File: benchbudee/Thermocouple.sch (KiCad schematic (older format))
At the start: 0 parts

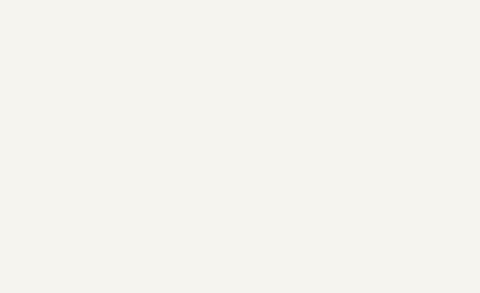
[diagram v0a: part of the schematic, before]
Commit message: Added signals
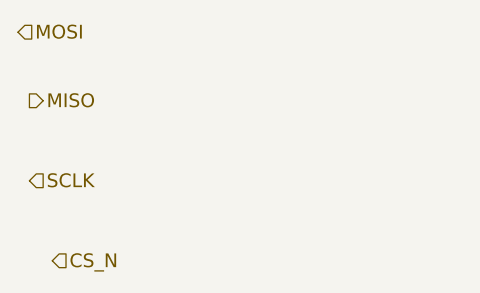
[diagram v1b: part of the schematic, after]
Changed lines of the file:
@@
 Text HLabel 8800 2850 2    60   Input ~ 0
 TC IN -
+Text HLabel 1650 2050 2    60   Input ~ 0
+MOSI
+Text HLabel 1700 2350 2    60   Output ~ 0
+MISO
+Text HLabel 1700 2700 2    60   Input ~ 0
+SCLK
+Text HLabel 1800 3050 2    60   Input ~ 0
+CS_N
 $EndSCHEMATC

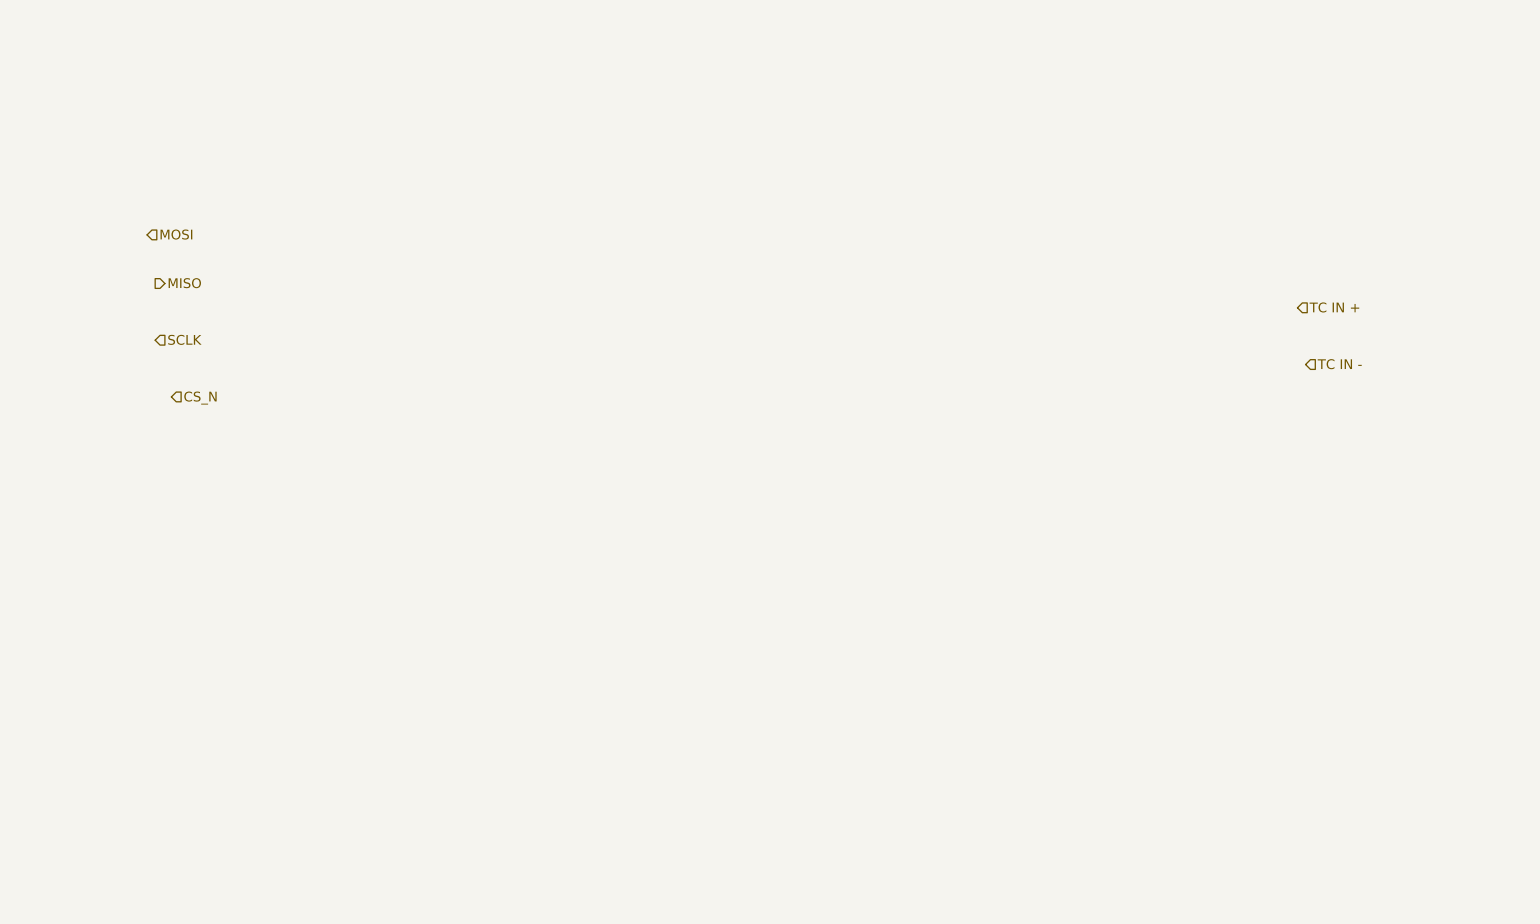
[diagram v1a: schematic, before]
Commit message: Added block diagram and thermocouple schematic
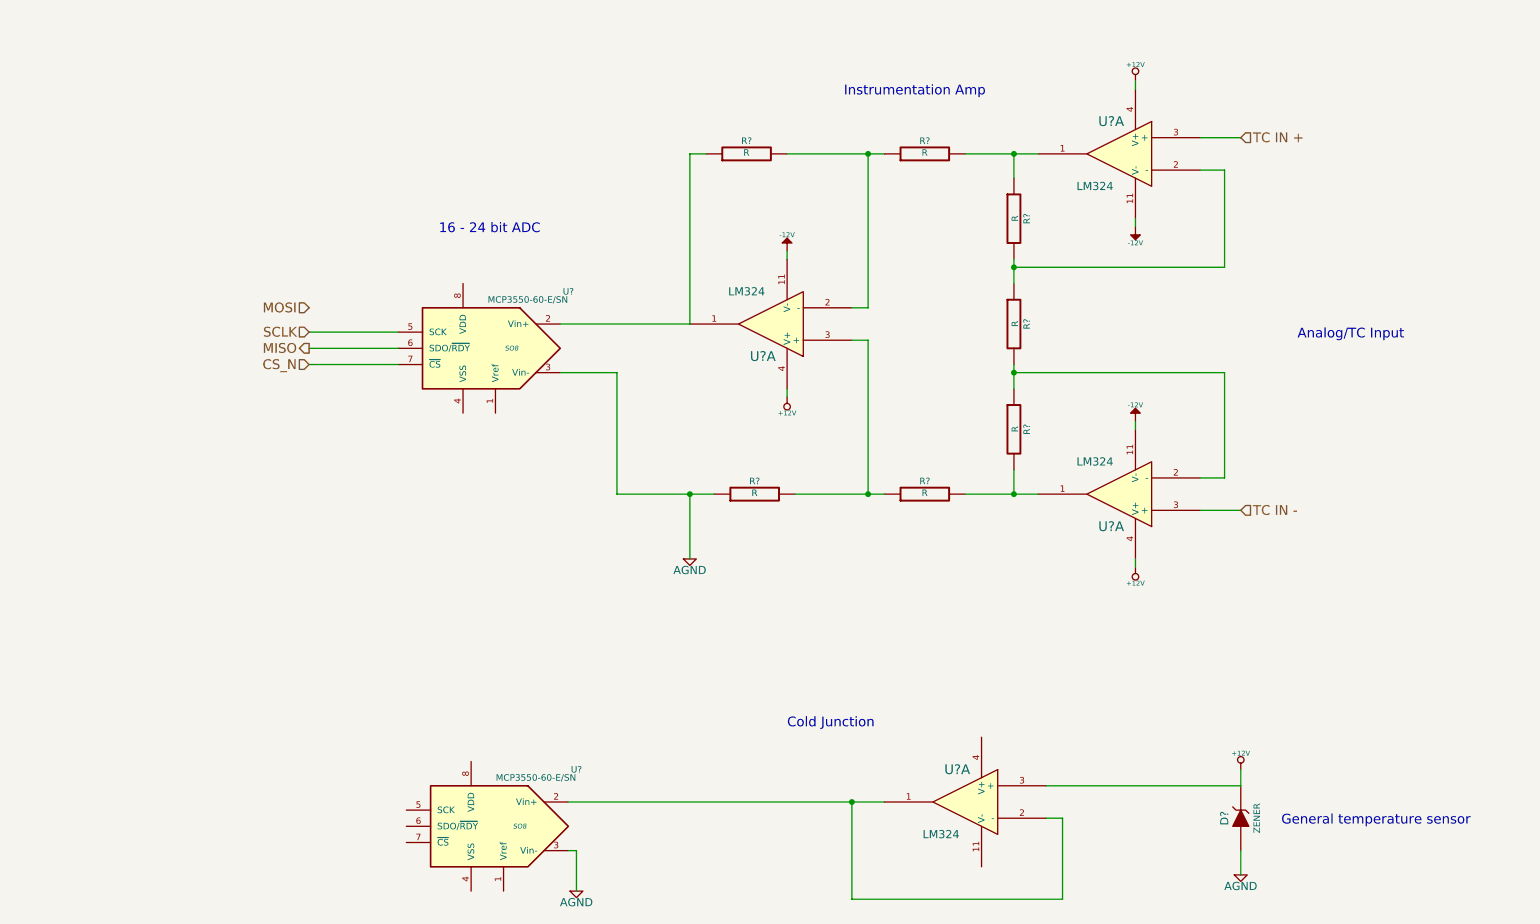
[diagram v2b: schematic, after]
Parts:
- added D?: ZENER, ~, symbol ZENER
- added R? (x7): R, ~, symbol R
- added U? (x4): LM324, symbol LM324
- added U? (x2): MCP3550-60-E/SN, SO8, symbol MCP3550-60-E/SN
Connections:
- net CS_N: now also U?.7 (~CS~)
- net MISO: now also U?.6 (SDO/~RDY~)
- net SCLK: now also U?.5 (SCK)
- net TC IN +: now also U?.3 (+)
- net TC IN -: now also U?.3 (+)
- new net: R?.1, R?.2, U?.1
- new net: R?.1, R?.2, U?.2 (-) (x3)
- new net: R?.2, R?.2, U?.1
- new net: R?.1, U?.1, U?.2 (Vin+)
- new net: R?.1, R?.2, U?.3 (+)
- new net: U?.1, U?.2 (-), U?.2 (Vin+)
- new net +12V: D?.2 (K), U?.3 (+), U?.4 (V+), U?.4 (V+), U?.4 (V+)
- new net -12V: U?.11 (V-), U?.11 (V-), U?.11 (V-)
- new net AGND: D?.1 (A), R?.1, U?.3 (Vin-), U?.3 (Vin-)
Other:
- note added: "16 - 24 bit ADC"
- note added: "Analog/TC Input"
- note added: "Cold Junction"
- note added: "General temperature sensor"
- note added: "Instrumentation Amp"

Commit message: Relay module footprints done
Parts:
- gave numbers to parts that had none: 11
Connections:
- net +12V: now also U4.5 (+); no longer U4.3 (+)
- net TC IN +: now also U4.10 (+); no longer U4.3 (+)
- net TC IN -: now also U4.12 (+); no longer U4.3 (+)
- net at R11.1, R9.2: now also U4.8; no longer U4.1
- net at R11.2, R12.1: now also U4.9 (-); no longer U4.2 (-)
- net at R10.2, R13.2: now also U4.14; no longer U4.1
- net at R12.2, R13.1: now also U4.13 (-); no longer U4.2 (-)
- new net: U3.2 (Vin+), U4.6 (-), U4.7
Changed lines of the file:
@@
 CS_N
 $Comp
-L LM324 U?
-U 1 1 52FAF263
+L LM324 U4
+U 3 1 52FAF263
 P 7650 1550
-F 0 "U?" H 7700 1750 60  0000 C CNN
+F 0 "U4" H 7700 1750 60  0000 C CNN
 F 1 "LM324" H 7800 1350 50  0000 C CNN
 F 2 "" H 7650 1550 60  0000 C CNN
 F 3 "" H 7650 1550 60  0000 C CNN
-	1    7650 1550
+	3    7650 1550
 	-1   0    0    -1
 $EndComp
 $Comp
-L LM324 U?
-U 1 1 52FAF27A
+L LM324 U4
+U 4 1 52FAF27A
 P 7650 3650
-F 0 "U?" H 7700 3850 60  0000 C CNN
+F 0 "U4" H 7700 3850 60  0000 C CNN
 F 1 "LM324" H 7800 3450 50  0000 C CNN
 F 2 "" H 7650 3650 60  0000 C CNN
 F 3 "" H 7650 3650 60  0000 C CNN
-	1    7650 3650
-	-1   0    0    1
-$EndComp
-$Comp
-L LM324 U?
+	4    7650 3650
+	-1   0    0    1
+$EndComp
+$Comp
+L LM324 U4
 U 1 1 52FAF280
 P 5500 2600
-F 0 "U?" H 5550 2800 60  0000 C CNN
+F 0 "U4" H 5550 2800 60  0000 C CNN
 F 1 "LM324" H 5650 2400 50  0000 C CNN
 F 2 "" H 5500 2600 60  0000 C CNN
@@
 $EndComp
 $Comp
-L LM324 U?
-U 1 1 52FAF286
+L LM324 U4
+U 2 1 52FAF286
 P 6700 5550
-F 0 "U?" H 6750 5750 60  0000 C CNN
+F 0 "U4" H 6750 5750 60  0000 C CNN
 F 1 "LM324" H 6850 5350 50  0000 C CNN
 F 2 "" H 6700 5550 60  0000 C CNN
 F 3 "" H 6700 5550 60  0000 C CNN
-	1    6700 5550
+	2    6700 5550
 	-1   0    0    -1
 $EndComp
 $Comp
-L R R?
+L R R12
 U 1 1 52FAF2B2
 P 7000 2600
-F 0 "R?" V 7080 2600 40  0000 C CNN
+F 0 "R12" V 7080 2600 40  0000 C CNN
 F 1 "R" V 7007 2601 40  0000 C CNN
 F 2 "~" V 6930 2600 30  0000 C CNN
@@
 $EndComp
 $Comp
-L R R?
+L R R11
 U 1 1 52FAF2BF
 P 7000 1950
-F 0 "R?" V 7080 1950 40  0000 C CNN
+F 0 "R11" V 7080 1950 40  0000 C CNN
 F 1 "R" V 7007 1951 40  0000 C CNN
 F 2 "~" V 6930 1950 30  0000 C CNN
@@
 $EndComp
 $Comp
-L R R?
+L R R13
 U 1 1 52FAF2CF
 P 7000 3250
-F 0 "R?" V 7080 3250 40  0000 C CNN
+F 0 "R13" V 7080 3250 40  0000 C CNN
 F 1 "R" V 7007 3251 40  0000 C CNN
 F 2 "~" V 6930 3250 30  0000 C CNN
@@
 $EndComp
 $Comp
-L R R?
+L R R9
 U 1 1 52FAF2EA
 P 6450 1550
-F 0 "R?" V 6530 1550 40  0000 C CNN
+F 0 "R9" V 6530 1550 40  0000 C CNN
 F 1 "R" V 6457 1551 40  0000 C CNN
 F 2 "~" V 6380 1550 30  0000 C CNN
@@
 $EndComp
 $Comp
-L R R?
+L R R7
 U 1 1 52FAF2F0
 P 5350 1550
-F 0 "R?" V 5430 1550 40  0000 C CNN
+F 0 "R7" V 5430 1550 40  0000 C CNN
 F 1 "R" V 5357 1551 40  0000 C CNN
 F 2 "~" V 5280 1550 30  0000 C CNN
@@
 $EndComp
 $Comp
-L R R?
+L R R8
 U 1 1 52FAF2F6
 P 5400 3650
-F 0 "R?" V 5480 3650 40  0000 C CNN
+F 0 "R8" V 5480 3650 40  0000 C CNN
 F 1 "R" V 5407 3651 40  0000 C CNN
 F 2 "~" V 5330 3650 30  0000 C CNN
@@
 $EndComp
 $Comp
-L R R?
+L R R10
 U 1 1 52FAF2FC
 P 6450 3650
-F 0 "R?" V 6530 3650 40  0000 C CNN
+F 0 "R10" V 6530 3650 40  0000 C CNN
 F 1 "R" V 6457 3651 40  0000 C CNN
 F 2 "~" V 6380 3650 30  0000 C CNN
@@
 $EndComp
 $Comp
-L -12V #PWR?
+L -12V #PWR01
 U 1 1 52FAF3D3
 P 5600 2150
-F 0 "#PWR?" H 5600 2280 20  0001 C CNN
+F 0 "#PWR01" H 5600 2280 20  0001 C CNN
 F 1 "-12V" H 5600 2250 30  0000 C CNN
 F 2 "" H 5600 2150 60  0000 C CNN
@@
 $EndComp
 $Comp
-L -12V #PWR?
+L -12V #PWR02
 U 1 1 52FAF3E0
 P 7750 2000
-F 0 "#PWR?" H 7750 2130 20  0001 C CNN
+F 0 "#PWR02" H 7750 2130 20  0001 C CNN
 F 1 "-12V" H 7750 2100 30  0000 C CNN
 F 2 "" H 7750 2000 60  0000 C CNN
@@
 $EndComp
 $Comp
-L -12V #PWR?
+L -12V #PWR03
 U 1 1 52FAF3E6
 P 7750 3200
-F 0 "#PWR?" H 7750 3330 20  0001 C CNN
+F 0 "#PWR03" H 7750 3330 20  0001 C CNN
 F 1 "-12V" H 7750 3300 30  0000 C CNN
 F 2 "" H 7750 3200 60  0000 C CNN
@@
 $EndComp
 $Comp
-L +12V #PWR?
+L +12V #PWR04
 U 1 1 52FBAE4E
 P 5600 3050
-F 0 "#PWR?" H 5600 3000 20  0001 C CNN
+F 0 "#PWR04" H 5600 3000 20  0001 C CNN
 F 1 "+12V" H 5600 3150 30  0000 C CNN
 F 2 "" H 5600 3050 60  0000 C CNN
@@
 $EndComp
 $Comp
-L +12V #PWR?
+L +12V #PWR05
 U 1 1 52FBAE5B
 P 7750 4100
-F 0 "#PWR?" H 7750 4050 20  0001 C CNN
+F 0 "#PWR05" H 7750 4050 20  0001 C CNN
 F 1 "+12V" H 7750 4200 30  0000 C CNN
 F 2 "" H 7750 4100 60  0000 C CNN
@@
 $EndComp
 $Comp
-L +12V #PWR?
+L +12V #PWR06
 U 1 1 52FBAE63
 P 7750 1100
-F 0 "#PWR?" H 7750 1050 20  0001 C CNN
+F 0 "#PWR06" H 7750 1050 20  0001 C CNN
 F 1 "+12V" H 7750 1200 30  0000 C CNN
 F 2 "" H 7750 1100 60  0000 C CNN
@@
 $EndComp
 $Comp
-L AGND #PWR?
+L AGND #PWR07
 U 1 1 52FBAED0
 P 5000 4050
-F 0 "#PWR?" H 5000 4050 40  0001 C CNN
+F 0 "#PWR07" H 5000 4050 40  0001 C CNN
 F 1 "AGND" H 5000 3980 50  0000 C CNN
 F 2 "" H 5000 4050 60  0000 C CNN
@@
 $EndComp
 Wire Wire Line
-	6700 1550 7000 1550
-Wire Wire Line
-	7000 1550 7150 1550
+	6700 1550 7150 1550
 Wire Wire Line
 	7000 1550 7000 1700
 Wire Wire Line
-	7000 2200 7000 2250
-Wire Wire Line
-	7000 2250 7000 2350
-Wire Wire Line
-	7000 2850 7000 2900
-Wire Wire Line
-	7000 2900 7000 3000
+	7000 2200 7000 2350
+Wire Wire Line
+	7000 2850 7000 3000
 Wire Wire Line
 	7000 3500 7000 3650
 Wire Wire Line
-	6700 3650 7000 3650
-Wire Wire Line
-	7000 3650 7150 3650
+	6700 3650 7150 3650
 Connection ~ 7000 1550
 Connection ~ 7000 3650
 Wire Wire Line
-	5600 1550 6100 1550
-Wire Wire Line
-	6100 1550 6200 1550
+	5600 1550 6200 1550
 Wire Wire Line
 	6100 1550 6100 2500
@@
 	6100 2700 6100 3650
 Wire Wire Line
-	5650 3650 6100 3650
-Wire Wire Line
-	6100 3650 6200 3650
+	5650 3650 6200 3650
 Connection ~ 6100 3650
 Wire Wire Line
@@
 	5600 3050 5600 3000
 Wire Wire Line
-	4550 3650 5000 3650
-Wire Wire Line
-	5000 3650 5150 3650
+	4550 3650 5150 3650
 Wire Wire Line
 	5000 3650 5000 4050
 $Comp
-L MCP3550-60-E/SN U?
+L MCP3550-60-E/SN U2
 U 1 1 52FBAFBC
 P 3700 2750
-F 0 "U?" H 3150 3100 40  0000 C CNN
+F 0 "U2" H 3150 3100 40  0000 C CNN
 F 1 "MCP3550-60-E/SN" H 3400 3050 40  0000 C CNN
 F 2 "SO8" H 3500 2750 30  0000 C CIN
@@
 Connection ~ 7000 2900
 $Comp
-L MCP3550-60-E/SN U?
+L MCP3550-60-E/SN U3
 U 1 1 52FBB191
 P 3750 5700
-F 0 "U?" H 3200 6050 40  0000 C CNN
+F 0 "U3" H 3200 6050 40  0000 C CNN
 F 1 "MCP3550-60-E/SN" H 3450 6000 40  0000 C CNN
 F 2 "SO8" H 3550 5700 30  0000 C CIN
@@
 $EndComp
 $Comp
-L ZENER D?
+L ZENER D3
 U 1 1 52FBB1E7
 P 8400 5650
-F 0 "D?" H 8400 5750 50  0000 C CNN
+F 0 "D3" H 8400 5750 50  0000 C CNN
 F 1 "ZENER" H 8400 5550 40  0000 C CNN
 F 2 "~" H 8400 5650 60  0000 C CNN
@@
 $EndComp
 $Comp
-L +12V #PWR?
+L +12V #PWR08
 U 1 1 52FBB1F9
 P 8400 5350
-F 0 "#PWR?" H 8400 5300 20  0001 C CNN
+F 0 "#PWR08" H 8400 5300 20  0001 C CNN
 F 1 "+12V" H 8400 5450 30  0000 C CNN
 F 2 "" H 8400 5350 60  0000 C CNN
@@
 $EndComp
 $Comp
-L AGND #PWR?
+L AGND #PWR09
 U 1 1 52FBB1FF
 P 8400 6000
-F 0 "#PWR?" H 8400 6000 40  0001 C CNN
+F 0 "#PWR09" H 8400 6000 40  0001 C CNN
 F 1 "AGND" H 8400 5930 50  0000 C CNN
 F 2 "" H 8400 6000 60  0000 C CNN
@@
 	8400 5850 8400 6000
 Wire Wire Line
-	4250 5550 6000 5550
-Wire Wire Line
-	6000 5550 6200 5550
+	4250 5550 6200 5550
 Wire Wire Line
 	8400 5450 7200 5450
@@
 	4300 5850 4300 6100
 $Comp
-L AGND #PWR?
+L AGND #PWR010
 U 1 1 52FBB3F3
 P 4300 6100
-F 0 "#PWR?" H 4300 6100 40  0001 C CNN
+F 0 "#PWR010" H 4300 6100 40  0001 C CNN
 F 1 "AGND" H 4300 6030 50  0000 C CNN
 F 2 "" H 4300 6100 60  0000 C CNN

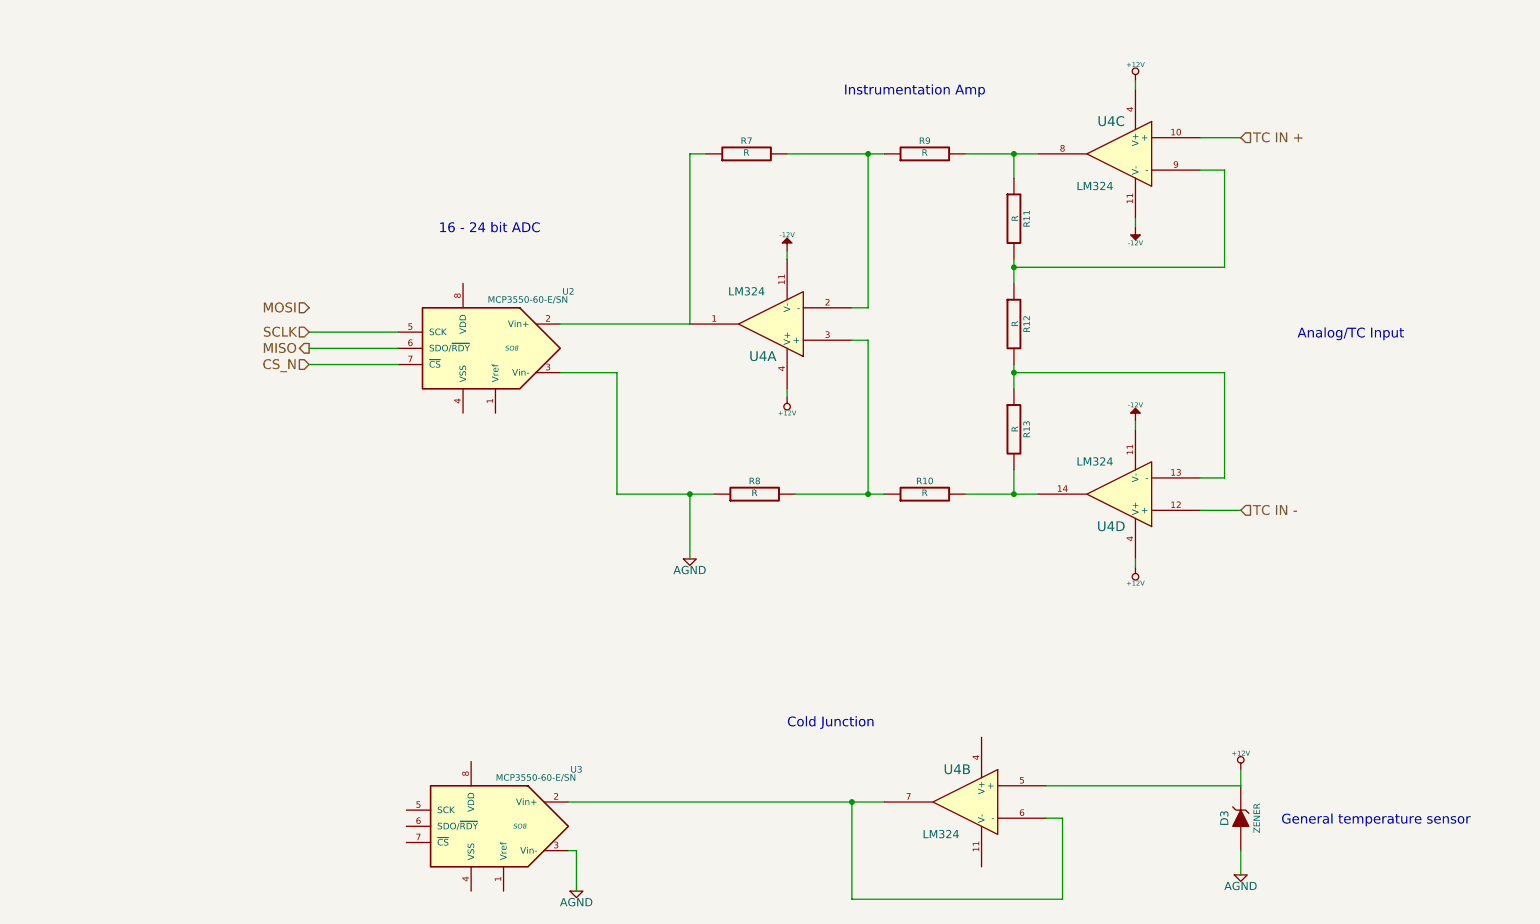
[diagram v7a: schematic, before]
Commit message: Schematic and associations for the thermocouple module
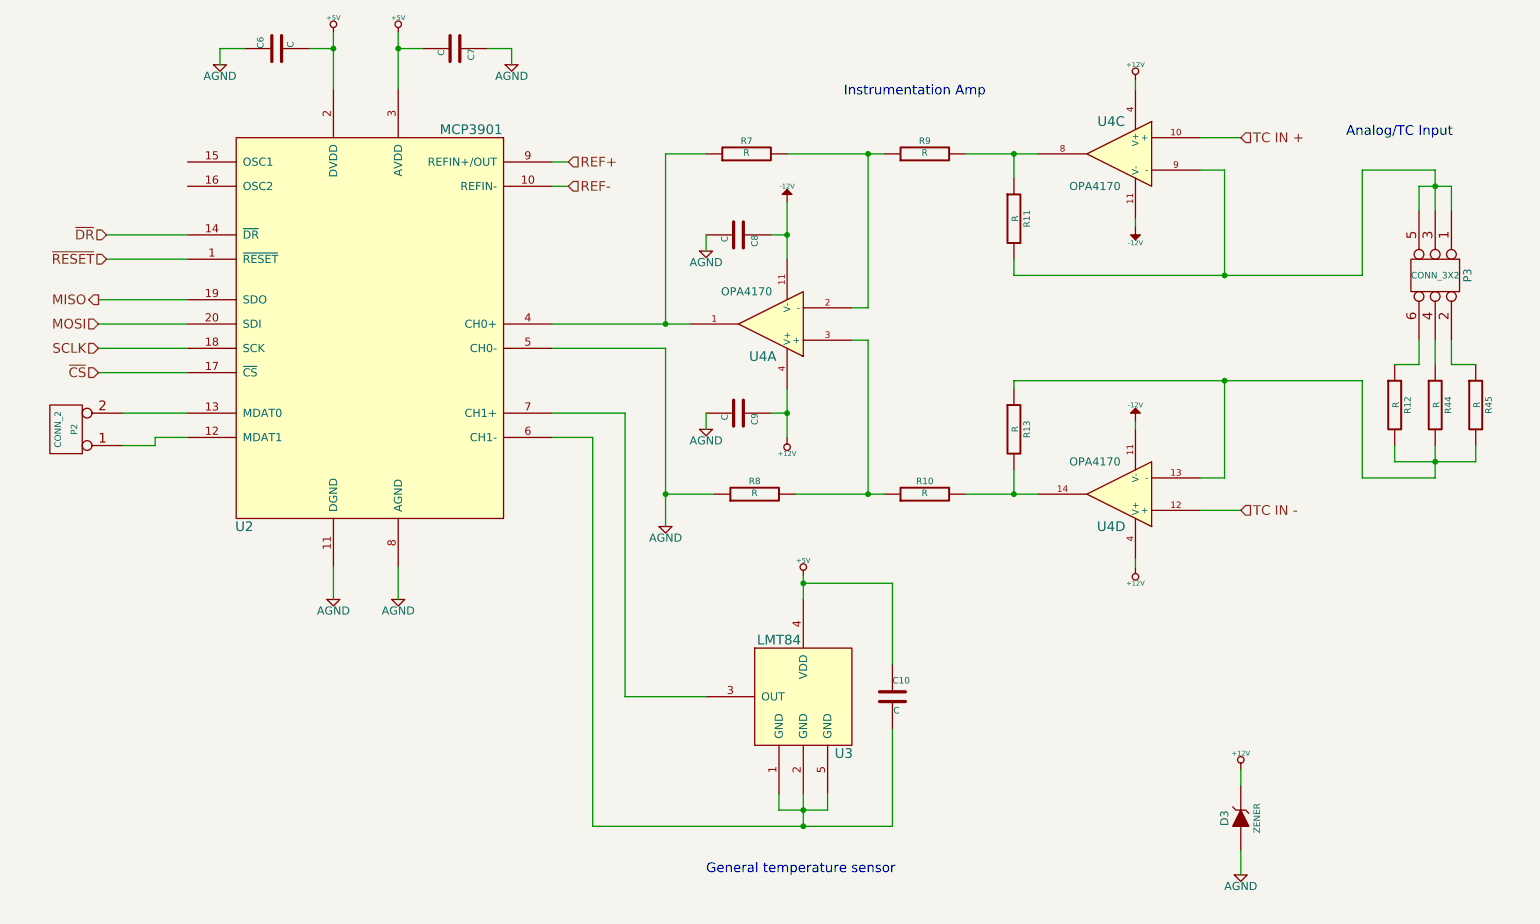
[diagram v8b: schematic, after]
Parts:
- removed U2, U3: MCP3550-60-E/SN, SO8, symbol MCP3550-60-E/SN
- removed unit 2 of U4
- added C10, C6, C7, C8, C9: C, symbol C
- added P2: CONN_2, symbol CONN_2
- added P3: CONN_3X2, symbol CONN_3X2
- added R44, R45: R, ~, symbol R
- added U2: MCP3901, symbol MCP3901
- added U3: LMT84, symbol LMT84
- U4: value LM324 -> OPA4170
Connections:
- net +12V: now also C9.1
- net -12V: now also C8.1
- net AGND: now also C6.1, C7.1, C8.2, C9.2, U2.11 (DGND), U2.5 (CH0-), U2.8 (AGND)
- net MISO: now also U2.19 (SDO)
- net MOSI: now also U2.20 (SDI)
- net SCLK: now also U2.18 (SCK)
- net at R11.2, U4.9 (-): now also P3.1, P3.3, P3.5; no longer R12.1
- net at R12.2, R13.1, U4.13 (-): now also R44.2, R45.2
- net at R7.1, U4.1: now also U2.4 (CH0+)
- new net: P3.6, R12.1
- new net: P2.1 (P1), U2.12 (MDAT1)
- new net: P2.2 (PM), U2.13 (MDAT0)
- new net: C10.2, U2.6 (CH1-), U3.1 (GND), U3.2 (GND), U3.5 (GND)
- new net: U2.7 (CH1+), U3.3 (OUT)
- new net: P3.4, R44.1
- new net: P3.2, R45.1
- new net +5V: C10.1, C6.2, C7.2, U2.2 (DVDD), U2.3 (AVDD), U3.4 (VDD)
- new net REF+: U2.9 (REFIN+/OUT)
- new net REF-: U2.10 (REFIN-)
- new net ~CS: U2.17 (~CS)
- new net ~DR: U2.14 (~DR)
- new net ~RESET: U2.1 (~RESET)
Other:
- note removed: "16 - 24 bit ADC"
- note removed: "Cold Junction"
- moved on the sheet: R12
